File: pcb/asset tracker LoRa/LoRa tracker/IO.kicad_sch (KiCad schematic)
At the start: 9 parts, among them J2 Screw_Terminal_01x02, Q1 BSS138, U4 G3VM-61HR2(TR05), U5 DS28CM00R-A00+T

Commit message: pcb kastje
pcb in kastje getekend
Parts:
- added C28, C30: 100nF, vanalles:0603, symbol Device:C_Small
- added C29, C31: 10uF, vanalles:0603, symbol Device:C_Small
- added U9: ATECC608B, halfgeleiders:soic p1.27 lengt 5.40, symbol Halfgelijders:ATECC608B
- Q1: footprint halfgeleiders:sop4 P=2.54 -> halfgeleiders:sot-23,
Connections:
- net +3V3: now also C28.1, C29.1, C30.1, C31.1, U9.8 (VCC)
- net GND: now also C28.2, C29.2, C30.2, C31.2, U9.4 (GND)
- new net SCL_CRYPTO: U9.6 (SCL)
- new net SDA_CRYPTO: U9.5 (SDA)
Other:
- note added: "crypto chip"

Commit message: klaar
print hertekend naar stm32L5
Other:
- note added: "sound"
- moved on the sheet: C28, C29, C30, C31, U9

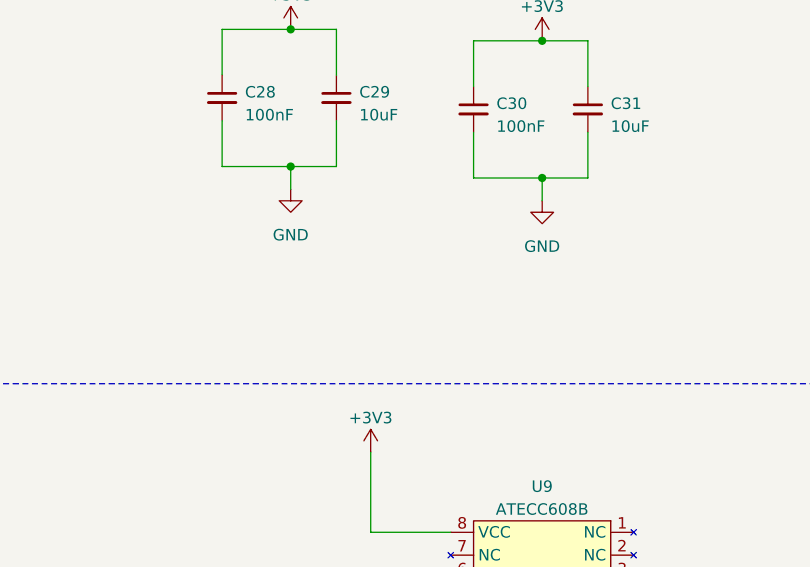
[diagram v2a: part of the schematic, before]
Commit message: versie2
aan versie 2 begonnen met tekenen en code beginnen schrijven voor quadkey
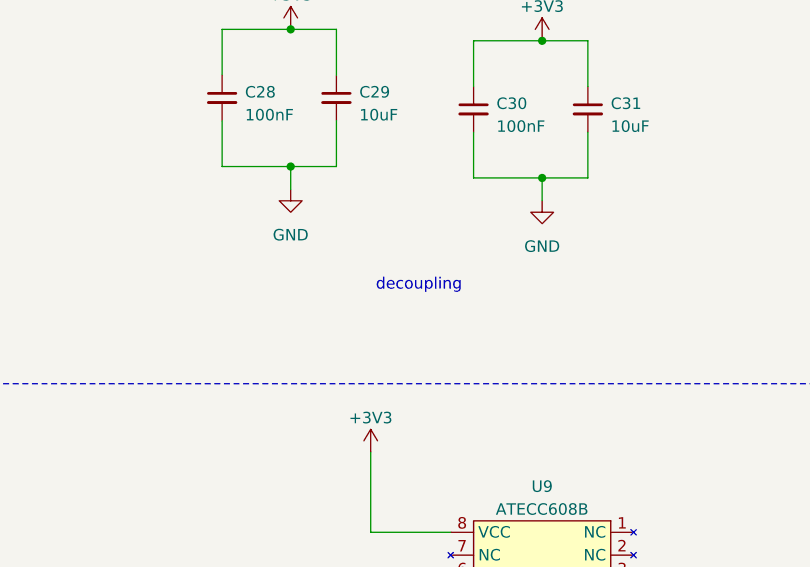
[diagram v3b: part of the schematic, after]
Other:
- note added: "decoupling"
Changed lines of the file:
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@@
+    (effects (font (size 1.27 1.27)) (justify right bottom))
+  )
+  (text "decoupling\n" (at 233.68 53.34 180)
     (effects (font (size 1.27 1.27)) (justify right bottom))
   )
